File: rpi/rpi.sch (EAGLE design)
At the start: 20 parts, among them IC1 MCP2515-E/SO, IC2 MCP2551, IC3 LM2595NDH

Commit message: Added power injector board; refactored boards to use MCP2562 instead of MCP2551
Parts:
- removed R2: 18k, SparkFun-Passives:RESISTOR0603-RES
- removed R3: 10k, SparkFun-Passives:RESISTOR0603-RES
- removed R4: DNP, SparkFun-Passives:RESISTOR0603-RES
- added C7: 0.1u, SparkFun-Passives:CAP0603-CAP
- IC2: value MCP2551 -> MCP2562; device SparkFun-DigitalIC:MCP2551 -> nickparts:MCP2562
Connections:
- removed net N$1: IC2.RXD, R3.2
- removed net N$8: IC2.RS, R4.2
- net +3V3: now also C7.1, IC2.VIO
- net GND: now also C7.2, IC2.STBY; no longer R2.1, R4.1
- net N$2: now also IC2.RXD; no longer R2.2, R3.1
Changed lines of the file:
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@@
 <part name="U$3" library="SparkFun-Connectors" deviceset="RJ45-8" device="PTH"/>
 <part name="IC1" library="mcp2515" deviceset="MCP2515" device="-E/SO"/>
-<part name="IC2" library="SparkFun-DigitalIC" deviceset="MCP2551" device=""/>
+<part name="IC2" library="nickparts" deviceset="MCP2562" device=""/>
 <part name="+3V1" library="supply1" deviceset="+3V3" device=""/>
 <part name="GND1" library="supply1" deviceset="GND" device=""/>
@@
 <part name="GND3" library="supply1" deviceset="GND" device=""/>
 <part name="+3V3" library="supply1" deviceset="+3V3" device=""/>
-<part name="R3" library="SparkFun-Passives" deviceset="RESISTOR" device="0603-RES" value="10k"/>
-<part name="R2" library="SparkFun-Passives" deviceset="RESISTOR" device="0603-RES" value="18k"/>
-<part name="GND4" library="supply1" deviceset="GND" device=""/>
 <part name="P+1" library="supply1" deviceset="+5V" device=""/>
 <part name="GND5" library="supply1" deviceset="GND" device=""/>
@@
 <part name="GND9" library="supply1" deviceset="GND" device=""/>
 <part name="GND10" library="supply1" deviceset="GND" device=""/>
-<part name="R4" library="SparkFun-Passives" deviceset="RESISTOR" device="0603-RES" value="DNP"/>
 <part name="GND11" library="supply1" deviceset="GND" device=""/>
+<part name="+3V4" library="supply1" deviceset="+3V3" device=""/>
+<part name="C7" library="SparkFun-Passives" deviceset="CAP" device="0603-CAP" value="0.1u"/>
 </parts>
 <sheets>
@@
 <instance part="GND3" gate="1" x="165.1" y="15.24"/>
 <instance part="+3V3" gate="G$1" x="165.1" y="63.5"/>
-<instance part="R3" gate="G$1" x="198.12" y="38.1"/>
-<instance part="R2" gate="G$1" x="190.5" y="30.48" rot="R90"/>
-<instance part="GND4" gate="1" x="190.5" y="20.32"/>
 <instance part="P+1" gate="1" x="205.74" y="63.5"/>
 <instance part="GND5" gate="1" x="208.28" y="30.48"/>
@@
 <instance part="GND9" gate="1" x="200.66" y="48.26"/>
 <instance part="GND10" gate="1" x="170.18" y="48.26"/>
-<instance part="R4" gate="G$1" x="251.46" y="30.48" rot="R90"/>
 <instance part="GND11" gate="1" x="251.46" y="22.86"/>
+<instance part="+3V4" gate="G$1" x="248.92" y="53.34"/>
+<instance part="C7" gate="G$1" x="256.54" y="43.18"/>
 </instances>
 <busses>
@@
 <wire x1="170.18" y1="58.42" x2="165.1" y2="58.42" width="0.1524" layer="91"/>
 <junction x="165.1" y="58.42"/>
+</segment>
+<segment>
+<pinref part="IC2" gate="G$1" pin="VIO"/>
+<pinref part="+3V4" gate="G$1" pin="+3V3"/>
+<wire x1="241.3" y1="38.1" x2="248.92" y2="38.1" width="0.1524" layer="91"/>
+<wire x1="248.92" y1="38.1" x2="248.92" y2="48.26" width="0.1524" layer="91"/>
+<pinref part="C7" gate="G$1" pin="1"/>
+<wire x1="248.92" y1="48.26" x2="248.92" y2="50.8" width="0.1524" layer="91"/>
+<wire x1="256.54" y1="48.26" x2="248.92" y2="48.26" width="0.1524" layer="91"/>
+<junction x="248.92" y="48.26"/>
 </segment>
 </net>
@@
 <wire x1="162.56" y1="20.32" x2="165.1" y2="20.32" width="0.1524" layer="91"/>
 <wire x1="165.1" y1="20.32" x2="165.1" y2="17.78" width="0.1524" layer="91"/>
-</segment>
-<segment>
-<pinref part="R2" gate="G$1" pin="1"/>
-<pinref part="GND4" gate="1" pin="GND"/>
-<wire x1="190.5" y1="25.4" x2="190.5" y2="22.86" width="0.1524" layer="91"/>
 </segment>
 <segment>
@@
 </segment>
 <segment>
-<pinref part="R4" gate="G$1" pin="1"/>
+<pinref part="IC2" gate="G$1" pin="STBY"/>
+<wire x1="241.3" y1="45.72" x2="251.46" y2="45.72" width="0.1524" layer="91"/>
+<wire x1="251.46" y1="45.72" x2="251.46" y2="40.64" width="0.1524" layer="91"/>
 <pinref part="GND11" gate="1" pin="GND"/>
+<wire x1="251.46" y1="40.64" x2="251.46" y2="35.56" width="0.1524" layer="91"/>
+<wire x1="251.46" y1="25.4" x2="251.46" y2="35.56" width="0.1524" layer="91"/>
+<pinref part="C7" gate="G$1" pin="2"/>
+<wire x1="256.54" y1="40.64" x2="251.46" y2="40.64" width="0.1524" layer="91"/>
+<junction x="251.46" y="40.64"/>
 </segment>
 </net>
@@
 </segment>
 </net>
-<net name="N$1" class="0">
-<segment>
-<pinref part="IC2" gate="G$1" pin="RXD"/>
-<pinref part="R3" gate="G$1" pin="2"/>
-<wire x1="210.82" y1="38.1" x2="203.2" y2="38.1" width="0.1524" layer="91"/>
-</segment>
-</net>
 <net name="N$2" class="0">
 <segment>
-<pinref part="R3" gate="G$1" pin="1"/>
-<pinref part="R2" gate="G$1" pin="2"/>
 <wire x1="193.04" y1="38.1" x2="190.5" y2="38.1" width="0.1524" layer="91"/>
-<wire x1="190.5" y1="38.1" x2="190.5" y2="35.56" width="0.1524" layer="91"/>
 <wire x1="190.5" y1="38.1" x2="190.5" y2="43.18" width="0.1524" layer="91"/>
-<junction x="190.5" y="38.1"/>
 <pinref part="IC1" gate="G$1" pin="RXCAN"/>
 <wire x1="190.5" y1="43.18" x2="162.56" y2="43.18" width="0.1524" layer="91"/>
+<pinref part="IC2" gate="G$1" pin="RXD"/>
+<wire x1="210.82" y1="38.1" x2="203.2" y2="38.1" width="0.1524" layer="91"/>
+<wire x1="193.04" y1="38.1" x2="203.2" y2="38.1" width="0.1524" layer="91"/>
 </segment>
 </net>
@@
 </segment>
 </net>
-<net name="N$8" class="0">
-<segment>
-<pinref part="IC2" gate="G$1" pin="RS"/>
-<pinref part="R4" gate="G$1" pin="2"/>
-<wire x1="241.3" y1="45.72" x2="251.46" y2="45.72" width="0.1524" layer="91"/>
-<wire x1="251.46" y1="45.72" x2="251.46" y2="35.56" width="0.1524" layer="91"/>
-</segment>
-</net>

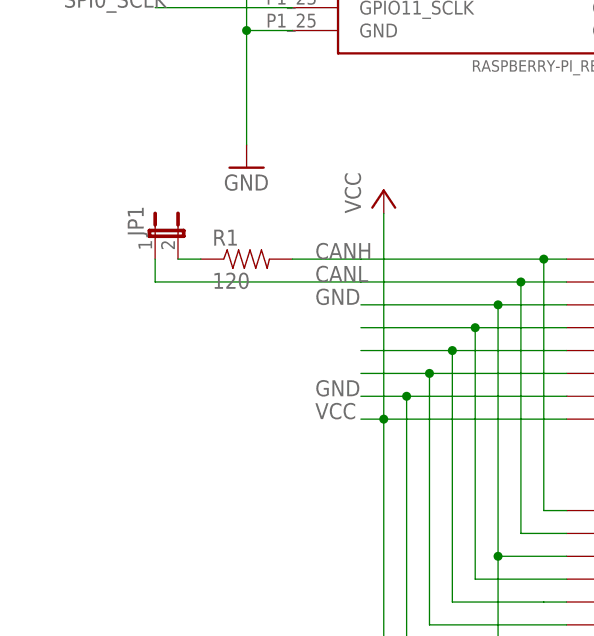
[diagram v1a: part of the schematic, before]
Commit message: Switch to split termination with a switch
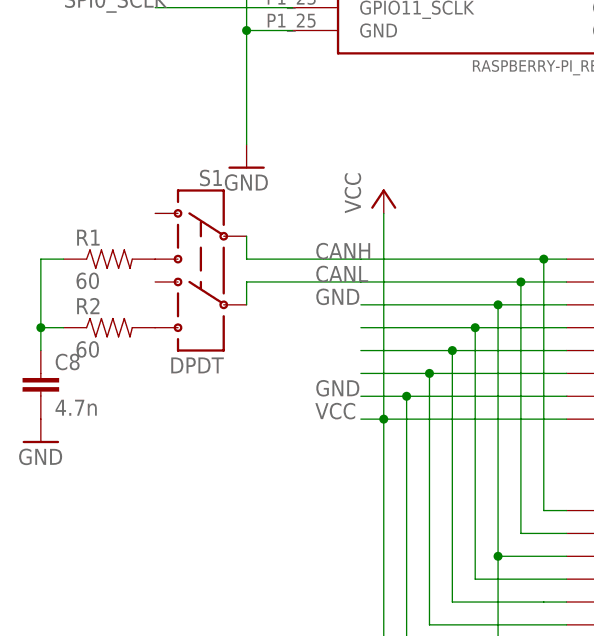
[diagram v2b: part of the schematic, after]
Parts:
- removed JP1: (no value), SparkFun-Passives:JUMPER-2PTH
- added C8: 4.7n, SparkFun-Passives:CAP0603-CAP
- added R2: 60, SparkFun-Passives:RESISTOR0603-RES
- added S1: DPDT, SparkFun-Electromechanical:SWITCH-DPDTAYZ0202
- R1: value 120 -> 60
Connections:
- new net N$1: R1.2, S1.3
- new net N$8: C8.1, R1.1, R2.1
- net CANH: now also S1.2; no longer R1.2
- net CANL: now also S1.5; no longer JP1.1
- net GND: now also C8.2
- net N$7: now also R2.2, S1.6; no longer JP1.2, R1.1
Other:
- moved on the sheet: R1
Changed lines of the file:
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@@
 <part name="GND8" library="supply1" deviceset="GND" device=""/>
 <part name="P+5" library="supply1" deviceset="VCC" device=""/>
-<part name="JP1" library="SparkFun-Passives" deviceset="JUMPER-2" device="PTH"/>
-<part name="R1" library="SparkFun-Passives" deviceset="RESISTOR" device="0603-RES" value="120"/>
+<part name="R1" library="SparkFun-Passives" deviceset="RESISTOR" device="0603-RES" value="60"/>
 <part name="C5" library="SparkFun-Passives" deviceset="CAP" device="0603-CAP" value="0.1u"/>
 <part name="C6" library="SparkFun-Passives" deviceset="CAP" device="0603-CAP" value="0.1u"/>
@@
 <part name="+3V4" library="supply1" deviceset="+3V3" device=""/>
 <part name="C7" library="SparkFun-Passives" deviceset="CAP" device="0603-CAP" value="0.1u"/>
+<part name="S1" library="SparkFun-Electromechanical" deviceset="SWITCH-DPDT" device="AYZ0202" value="DPDT"/>
+<part name="R2" library="SparkFun-Passives" deviceset="RESISTOR" device="0603-RES" value="60"/>
+<part name="C8" library="SparkFun-Passives" deviceset="CAP" device="0603-CAP" value="4.7n"/>
+<part name="GND4" library="supply1" deviceset="GND" device=""/>
 </parts>
 <sheets>
@@
 <instance part="GND8" gate="1" x="38.1" y="-53.34"/>
 <instance part="P+5" gate="VCC" x="25.4" y="7.62"/>
-<instance part="JP1" gate="A" x="0" y="2.54"/>
-<instance part="R1" gate="G$1" x="10.16" y="0"/>
+<instance part="R1" gate="G$1" x="-5.08" y="0"/>
 <instance part="C5" gate="G$1" x="170.18" y="53.34"/>
 <instance part="C6" gate="G$1" x="200.66" y="53.34"/>
@@
 <instance part="+3V4" gate="G$1" x="248.92" y="53.34"/>
 <instance part="C7" gate="G$1" x="256.54" y="43.18"/>
+<instance part="S1" gate="G$1" x="5.08" y="0" rot="MR0"/>
+<instance part="R2" gate="G$1" x="-5.08" y="-7.62"/>
+<instance part="C8" gate="G$1" x="-12.7" y="-15.24"/>
+<instance part="GND4" gate="1" x="-12.7" y="-20.32"/>
 </instances>
 <busses>
@@
 <junction x="251.46" y="40.64"/>
 </segment>
+<segment>
+<pinref part="C8" gate="G$1" pin="2"/>
+<pinref part="GND4" gate="1" pin="GND"/>
+</segment>
 </net>
 <net name="SPI0_CE0" class="0">
@@
 <junction x="43.18" y="0"/>
 <label x="17.78" y="0" size="1.778" layer="95"/>
-<pinref part="R1" gate="G$1" pin="2"/>
-<wire x1="22.86" y1="0" x2="15.24" y2="0" width="0.1524" layer="91"/>
+<pinref part="S1" gate="G$1" pin="2"/>
+<wire x1="22.86" y1="0" x2="10.16" y2="0" width="0.1524" layer="91"/>
+<wire x1="10.16" y1="0" x2="10.16" y2="2.54" width="0.1524" layer="91"/>
 </segment>
 </net>
@@
 <junction x="40.64" y="-2.54"/>
 <label x="17.78" y="-2.54" size="1.778" layer="95"/>
-<pinref part="JP1" gate="A" pin="1"/>
-<wire x1="22.86" y1="-2.54" x2="0" y2="-2.54" width="0.1524" layer="91"/>
-<wire x1="0" y1="-2.54" x2="0" y2="0" width="0.1524" layer="91"/>
+<pinref part="S1" gate="G$1" pin="5"/>
+<wire x1="22.86" y1="-2.54" x2="10.16" y2="-2.54" width="0.1524" layer="91"/>
+<wire x1="10.16" y1="-2.54" x2="10.16" y2="-5.08" width="0.1524" layer="91"/>
 </segment>
 </net>
@@
 </segment>
 </net>
+<net name="N$1" class="0">
+<segment>
+<pinref part="S1" gate="G$1" pin="3"/>
+<pinref part="R1" gate="G$1" pin="2"/>
+</segment>
+</net>
 <net name="N$7" class="0">
 <segment>
-<pinref part="JP1" gate="A" pin="2"/>
+<pinref part="S1" gate="G$1" pin="6"/>
+<pinref part="R2" gate="G$1" pin="2"/>
+</segment>
+</net>
+<net name="N$8" class="0">
+<segment>
 <pinref part="R1" gate="G$1" pin="1"/>
-<wire x1="2.54" y1="0" x2="5.08" y2="0" width="0.1524" layer="91"/>
-</segment>
-</net>
+<pinref part="C8" gate="G$1" pin="1"/>
+<wire x1="-10.16" y1="0" x2="-12.7" y2="0" width="0.1524" layer="91"/>
+<wire x1="-12.7" y1="0" x2="-12.7" y2="-7.62" width="0.1524" layer="91"/>
+<pinref part="R2" gate="G$1" pin="1"/>
+<wire x1="-12.7" y1="-7.62" x2="-12.7" y2="-10.16" width="0.1524" layer="91"/>
+<wire x1="-10.16" y1="-7.62" x2="-12.7" y2="-7.62" width="0.1524" layer="91"/>
+<junction x="-12.7" y="-7.62"/>
+</segment>
+</net>

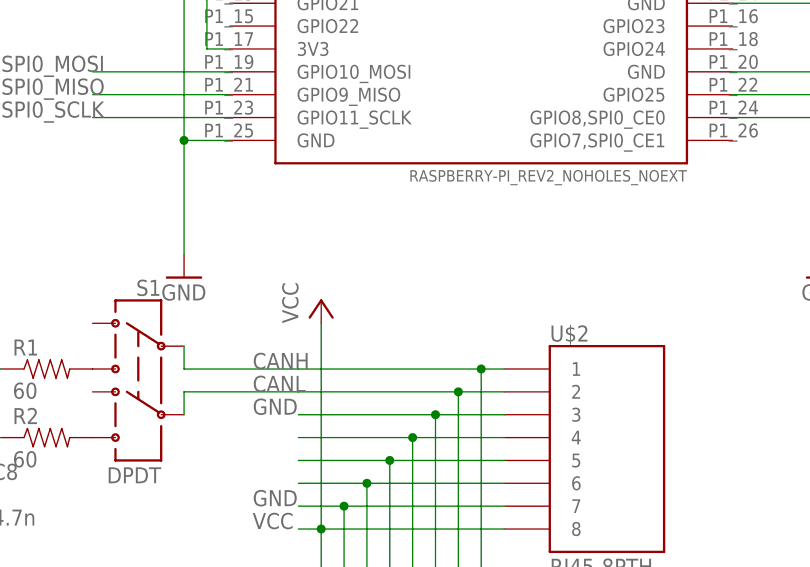
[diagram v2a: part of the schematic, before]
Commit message: Added TVS diodes, fixed silkscreen issues
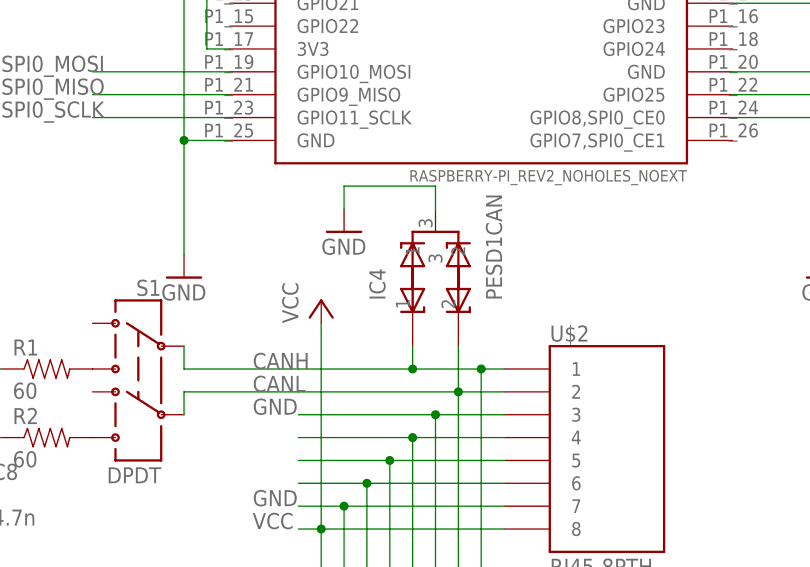
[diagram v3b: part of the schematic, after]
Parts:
- added IC4: PESD1CAN, nickparts:PESD1CAN
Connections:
- net CANH: now also IC4.1
- net CANL: now also IC4.2
- net GND: now also IC4.3
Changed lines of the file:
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@@
 <part name="C8" library="SparkFun-Passives" deviceset="CAP" device="0603-CAP" value="4.7n"/>
 <part name="GND4" library="supply1" deviceset="GND" device=""/>
+<part name="IC4" library="nickparts" deviceset="PESD1CAN" device=""/>
+<part name="GND12" library="supply1" deviceset="GND" device=""/>
 </parts>
 <sheets>
@@
 <instance part="C8" gate="G$1" x="-12.7" y="-15.24"/>
 <instance part="GND4" gate="1" x="-12.7" y="-20.32"/>
+<instance part="IC4" gate="G$1" x="38.1" y="15.24" rot="R90"/>
+<instance part="GND12" gate="1" x="27.94" y="15.24"/>
 </instances>
 <busses>
@@
 <pinref part="GND4" gate="1" pin="GND"/>
 </segment>
+<segment>
+<pinref part="IC4" gate="G$1" pin="3"/>
+<wire x1="38.1" y1="17.78" x2="38.1" y2="20.32" width="0.1524" layer="91"/>
+<pinref part="GND12" gate="1" pin="GND"/>
+<wire x1="38.1" y1="20.32" x2="27.94" y2="20.32" width="0.1524" layer="91"/>
+<wire x1="27.94" y1="20.32" x2="27.94" y2="17.78" width="0.1524" layer="91"/>
+</segment>
 </net>
 <net name="SPI0_CE0" class="0">
@@
 <pinref part="U$3" gate="G$1" pin="1"/>
 <wire x1="43.18" y1="-27.94" x2="45.72" y2="-27.94" width="0.1524" layer="91"/>
-<wire x1="43.18" y1="0" x2="22.86" y2="0" width="0.1524" layer="91"/>
+<wire x1="43.18" y1="0" x2="35.56" y2="0" width="0.1524" layer="91"/>
 <junction x="43.18" y="0"/>
 <label x="17.78" y="0" size="1.778" layer="95"/>
 <pinref part="S1" gate="G$1" pin="2"/>
+<wire x1="35.56" y1="0" x2="22.86" y2="0" width="0.1524" layer="91"/>
 <wire x1="22.86" y1="0" x2="10.16" y2="0" width="0.1524" layer="91"/>
 <wire x1="10.16" y1="0" x2="10.16" y2="2.54" width="0.1524" layer="91"/>
+<pinref part="IC4" gate="G$1" pin="1"/>
+<wire x1="35.56" y1="2.54" x2="35.56" y2="0" width="0.1524" layer="91"/>
+<junction x="35.56" y="0"/>
 </segment>
 </net>
@@
 <wire x1="22.86" y1="-2.54" x2="10.16" y2="-2.54" width="0.1524" layer="91"/>
 <wire x1="10.16" y1="-2.54" x2="10.16" y2="-5.08" width="0.1524" layer="91"/>
-</segment>
-</net>
+<pinref part="IC4" gate="G$1" pin="2"/>
+<wire x1="40.64" y1="2.54" x2="40.64" y2="-2.54" width="0.1524" layer="91"/>
+</segment>
+</net>

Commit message: Minor changes to shield, rpi board, and cape
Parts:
- removed L1: MSS1260, nickparts:MSS1260
- added C10: 56u, nickparts:10SVP56M
- added C9: 10n, nickparts:C0805C103K5RACTU
- added I1: SRN8040-330M, nickparts:SRN8040-330M
- C3: value (none) -> 4.7u; device SparkFun-Capacitors:CAP_POLG -> nickparts:GRM31CR71H475KA12L
- C4: value (none) -> 1u; device SparkFun-Capacitors:CAP_POLE -> nickparts:GMK212B7105KG-T
- D1: value (none) -> B240A-13-F; device SparkFun-DiscreteSemi:DIODESMA-ALT -> nickparts:B240A-13-F
- IC3: value LM2595NDH -> LM22675MR-5.0/NOPB; device nickparts:LM2595NDH -> nickparts:LM22675MR-5.0/NOPB
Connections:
- removed net N$10 (its old number): U$2.4, U$3.4
- removed net N$6: D1.C, IC3.OUT, L1.1
- new net N$9: U$2.3, U$3.3
- new net SWOUT: C9.2, D1.K, I1.2, IC3.SW
- net +5V: now also C10.+, I1.1; no longer C4.+, L1.2
- net GND: now also C10.-, C3.2, C4.2, U$2.8, U$3.8; no longer C3.-, C4.-, IC3./EN, U$2.3, U$3.3
- net N$11: now also C9.1, IC3.BOOT; no longer U$2.5, U$3.5
- net VCC: now also C3.1, C4.1, U$2.4, U$2.5, U$3.4, U$3.5; no longer C3.+, U$2.8, U$3.8
